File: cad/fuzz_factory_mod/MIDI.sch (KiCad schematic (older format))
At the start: 16 parts

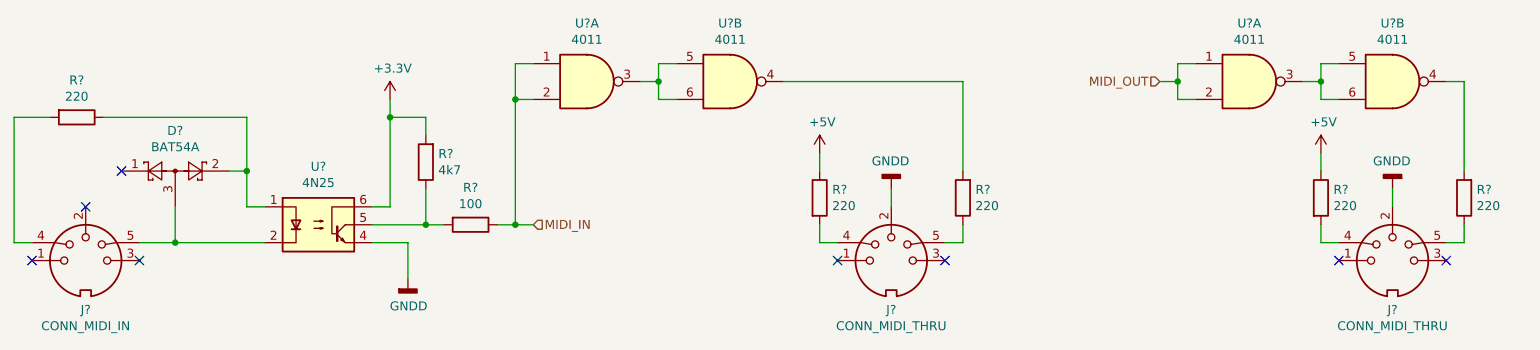
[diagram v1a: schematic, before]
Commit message: Continued schematic.
Modified fuuz_factory circuit : use of matched transistor pairs.
Added USB interface, through FT230X and direct to MCU.
Associated footprints, except for XTAL and trimmers.
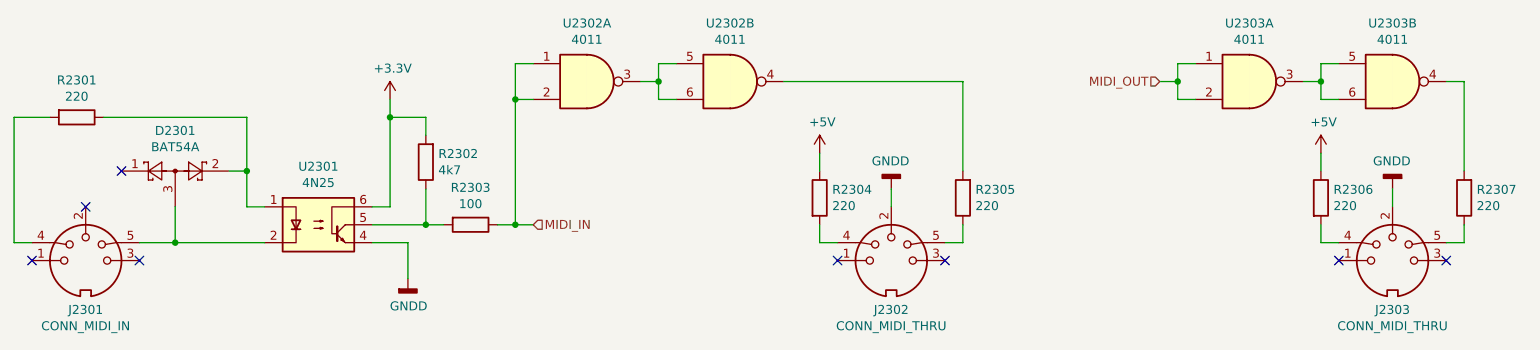
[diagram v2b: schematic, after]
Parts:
- J2301, J2302, J2303: renamed from J?; footprint (none) -> flax_lib:DIN5_through_hole
- R2301, R2304, R2305, R2306, R2307: renamed from R?; footprint (none) -> Resistors_SMD:R_0805
- R2302, R2303: renamed from R?; footprint (none) -> Resistors_SMD:R_0603
- U2302, U2303: renamed from U?; footprint (none) -> Housings_SOIC:SOIC-14_3.9x8.7mm_Pitch1.27mm
- gave numbers to parts that had none: 2
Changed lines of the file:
@@
 $Descr A4 11693 8268
 encoding utf-8
-Sheet 13 19
+Sheet 22 22
 Title ""
 Date ""
@@
 $EndDescr
 $Comp
-L Connector:DIN-5_180degree J?
+L Connector:DIN-5_180degree J2301
 U 1 1 5E67C58C
 P 2300 3500
-F 0 "J?" H 2300 3225 50  0000 C CNN
+F 0 "J2301" H 2300 3225 50  0000 C CNN
 F 1 "CONN_MIDI_IN" H 2300 3134 50  0000 C CNN
-F 2 "" H 2300 3500 50  0001 C CNN
+F 2 "flax_lib:DIN5_through_hole" H 2300 3500 50  0001 C CNN
 F 3 "http://www.mouser.com/ds/2/18/40_c091_abd_e-75918.pdf" H 2300 3500 50  0001 C CNN
 	1    2300 3500
@@
 $EndComp
 $Comp
-L Device:R R?
+L Device:R R2301
 U 1 1 5E67D871
 P 2250 2700
-F 0 "R?" V 2043 2700 50  0000 C CNN
+F 0 "R2301" V 2043 2700 50  0000 C CNN
 F 1 "220" V 2134 2700 50  0000 C CNN
-F 2 "" V 2180 2700 50  0001 C CNN
+F 2 "Resistors_SMD:R_0805" V 2180 2700 50  0001 C CNN
 F 3 "~" H 2250 2700 50  0001 C CNN
 	1    2250 2700
@@
 $EndComp
 $Comp
-L Diode:BAT54A D?
+L Diode:BAT54A D2301
 U 1 1 5E67E292
 P 2800 3000
-F 0 "D?" H 2800 3225 50  0000 C CNN
+F 0 "D2301" H 2800 3225 50  0000 C CNN
 F 1 "BAT54A" H 2800 3134 50  0000 C CNN
 F 2 "Package_TO_SOT_SMD:SOT-23" H 2875 3125 50  0001 L CNN
@@
 $EndComp
 $Comp
-L Isolator:4N25 U?
+L Isolator:4N25 U2301
 U 1 1 5E67F50F
 P 3600 3300
-F 0 "U?" H 3600 3625 50  0000 C CNN
+F 0 "U2301" H 3600 3625 50  0000 C CNN
 F 1 "4N25" H 3600 3534 50  0000 C CNN
 F 2 "Package_DIP:DIP-6_W7.62mm" H 3400 3100 50  0001 L CIN
@@
 Connection ~ 3200 3000
 $Comp
-L Device:R R?
+L Device:R R2302
 U 1 1 5E685D95
 P 4200 2950
-F 0 "R?" H 4130 2904 50  0000 R CNN
+F 0 "R2302" H 4130 2904 50  0000 R CNN
 F 1 "4k7" H 4130 2995 50  0000 R CNN
-F 2 "" V 4130 2950 50  0001 C CNN
+F 2 "Resistors_SMD:R_0603" V 4130 2950 50  0001 C CNN
 F 3 "~" H 4200 2950 50  0001 C CNN
 	1    4200 2950
@@
 $EndComp
 $Comp
-L Device:R R?
+L Device:R R2303
 U 1 1 5E6874F9
 P 4450 3300
-F 0 "R?" V 4243 3300 50  0000 C CNN
+F 0 "R2303" V 4243 3300 50  0000 C CNN
 F 1 "100" V 4334 3300 50  0000 C CNN
-F 2 "" V 4380 3300 50  0001 C CNN
+F 2 "Resistors_SMD:R_0603" V 4380 3300 50  0001 C CNN
 F 3 "~" H 4450 3300 50  0001 C CNN
 	1    4450 3300
@@
 	4200 3300 3900 3300
 $Comp
-L power:GNDD #PWR?
+L power:GNDD #PWR02302
 U 1 1 5E6887D9
 P 4100 3600
-F 0 "#PWR?" H 4100 3350 50  0001 C CNN
+F 0 "#PWR02302" H 4100 3350 50  0001 C CNN
 F 1 "GNDD" H 4104 3445 50  0000 C CNN
 F 2 "" H 4100 3600 50  0001 C CNN
@@
 	4600 3300 4700 3300
 $Comp
-L Connector:DIN-5_180degree J?
+L Connector:DIN-5_180degree J2302
 U 1 1 5E68C85A
 P 6800 3500
-F 0 "J?" H 6800 3225 50  0000 C CNN
+F 0 "J2302" H 6800 3225 50  0000 C CNN
 F 1 "CONN_MIDI_THRU" H 6800 3134 50  0000 C CNN
-F 2 "" H 6800 3500 50  0001 C CNN
+F 2 "flax_lib:DIN5_through_hole" H 6800 3500 50  0001 C CNN
 F 3 "http://www.mouser.com/ds/2/18/40_c091_abd_e-75918.pdf" H 6800 3500 50  0001 C CNN
 	1    6800 3500
@@
 $EndComp
 $Comp
-L 4xxx:4011 U?
+L 4xxx:4011 U2302
 U 1 1 5E68F415
 P 5100 2500
-F 0 "U?" H 5100 2825 50  0000 C CNN
+F 0 "U2302" H 5100 2825 50  0000 C CNN
 F 1 "4011" H 5100 2734 50  0000 C CNN
-F 2 "" H 5100 2500 50  0001 C CNN
+F 2 "Housings_SOIC:SOIC-14_3.9x8.7mm_Pitch1.27mm" H 5100 2500 50  0001 C CNN
 F 3 "http://www.intersil.com/content/dam/Intersil/documents/cd40/cd4011bms-12bms-23bms.pdf" H 5100 2500 50  0001 C CNN
 	1    5100 2500
@@
 $EndComp
 $Comp
-L 4xxx:4011 U?
+L 4xxx:4011 U2302
 U 2 1 5E692E59
 P 5900 2500
-F 0 "U?" H 5900 2825 50  0000 C CNN
+F 0 "U2302" H 5900 2825 50  0000 C CNN
 F 1 "4011" H 5900 2734 50  0000 C CNN
-F 2 "" H 5900 2500 50  0001 C CNN
+F 2 "Housings_SOIC:SOIC-14_3.9x8.7mm_Pitch1.27mm" H 5900 2500 50  0001 C CNN
 F 3 "http://www.intersil.com/content/dam/Intersil/documents/cd40/cd4011bms-12bms-23bms.pdf" H 5900 2500 50  0001 C CNN
 	2    5900 2500
@@
 	4700 3300 4800 3300
 $Comp
-L Device:R R?
+L Device:R R2304
 U 1 1 5E69AD62
 P 6400 3150
-F 0 "R?" H 6470 3196 50  0000 L CNN
+F 0 "R2304" H 6470 3196 50  0000 L CNN
 F 1 "220" H 6470 3105 50  0000 L CNN
-F 2 "" V 6330 3150 50  0001 C CNN
+F 2 "Resistors_SMD:R_0805" V 6330 3150 50  0001 C CNN
 F 3 "~" H 6400 3150 50  0001 C CNN
 	1    6400 3150
@@
 $EndComp
 $Comp
-L Device:R R?
+L Device:R R2305
 U 1 1 5E69C11A
 P 7200 3150
-F 0 "R?" H 7130 3104 50  0000 R CNN
+F 0 "R2305" H 7130 3104 50  0000 R CNN
 F 1 "220" H 7130 3195 50  0000 R CNN
-F 2 "" V 7130 3150 50  0001 C CNN
+F 2 "Resistors_SMD:R_0805" V 7130 3150 50  0001 C CNN
 F 3 "~" H 7200 3150 50  0001 C CNN
 	1    7200 3150
@@
 $EndComp
 $Comp
-L power:GNDD #PWR?
+L power:GNDD #PWR02304
 U 1 1 5E69CD49
 P 6800 3100
-F 0 "#PWR?" H 6800 2850 50  0001 C CNN
+F 0 "#PWR02304" H 6800 2850 50  0001 C CNN
 F 1 "GNDD" H 6804 2945 50  0000 C CNN
 F 2 "" H 6800 3100 50  0001 C CNN
@@
 	6400 3400 6500 3400
 $Comp
-L power:+5V #PWR?
+L power:+5V #PWR02303
 U 1 1 5E6A0890
 P 6400 2900
-F 0 "#PWR?" H 6400 2750 50  0001 C CNN
+F 0 "#PWR02303" H 6400 2750 50  0001 C CNN
 F 1 "+5V" H 6415 3073 50  0000 C CNN
 F 2 "" H 6400 2900 50  0001 C CNN
@@
 	7200 2500 7200 3000
 $Comp
-L 4xxx:4011 U?
+L 4xxx:4011 U2303
 U 1 1 5E6A2B71
 P 8800 2500
-F 0 "U?" H 8800 2825 50  0000 C CNN
+F 0 "U2303" H 8800 2825 50  0000 C CNN
 F 1 "4011" H 8800 2734 50  0000 C CNN
-F 2 "" H 8800 2500 50  0001 C CNN
+F 2 "Housings_SOIC:SOIC-14_3.9x8.7mm_Pitch1.27mm" H 8800 2500 50  0001 C CNN
 F 3 "http://www.intersil.com/content/dam/Intersil/documents/cd40/cd4011bms-12bms-23bms.pdf" H 8800 2500 50  0001 C CNN
 	1    8800 2500
@@
 $EndComp
 $Comp
-L 4xxx:4011 U?
+L 4xxx:4011 U2303
 U 2 1 5E6A2B7B
 P 9600 2500
-F 0 "U?" H 9600 2825 50  0000 C CNN
+F 0 "U2303" H 9600 2825 50  0000 C CNN
 F 1 "4011" H 9600 2734 50  0000 C CNN
-F 2 "" H 9600 2500 50  0001 C CNN
+F 2 "Housings_SOIC:SOIC-14_3.9x8.7mm_Pitch1.27mm" H 9600 2500 50  0001 C CNN
 F 3 "http://www.intersil.com/content/dam/Intersil/documents/cd40/cd4011bms-12bms-23bms.pdf" H 9600 2500 50  0001 C CNN
 	2    9600 2500
@@
 	9200 2500 9200 2600
 $Comp
-L Connector:DIN-5_180degree J?
+L Connector:DIN-5_180degree J2303
 U 1 1 5E6AB6C5
 P 9600 3500
-F 0 "J?" H 9600 3225 50  0000 C CNN
+F 0 "J2303" H 9600 3225 50  0000 C CNN
 F 1 "CONN_MIDI_THRU" H 9600 3134 50  0000 C CNN
-F 2 "" H 9600 3500 50  0001 C CNN
+F 2 "flax_lib:DIN5_through_hole" H 9600 3500 50  0001 C CNN
 F 3 "http://www.mouser.com/ds/2/18/40_c091_abd_e-75918.pdf" H 9600 3500 50  0001 C CNN
 	1    9600 3500
@@
 $EndComp
 $Comp
-L Device:R R?
+L Device:R R2306
 U 1 1 5E6AB6CF
 P 9200 3150
-F 0 "R?" H 9270 3196 50  0000 L CNN
+F 0 "R2306" H 9270 3196 50  0000 L CNN
 F 1 "220" H 9270 3105 50  0000 L CNN
-F 2 "" V 9130 3150 50  0001 C CNN
+F 2 "Resistors_SMD:R_0805" V 9130 3150 50  0001 C CNN
 F 3 "~" H 9200 3150 50  0001 C CNN
 	1    9200 3150
@@
 $EndComp
 $Comp
-L Device:R R?
+L Device:R R2307
 U 1 1 5E6AB6D9
 P 10000 3150
-F 0 "R?" H 9930 3104 50  0000 R CNN
+F 0 "R2307" H 9930 3104 50  0000 R CNN
 F 1 "220" H 9930 3195 50  0000 R CNN
-F 2 "" V 9930 3150 50  0001 C CNN
+F 2 "Resistors_SMD:R_0805" V 9930 3150 50  0001 C CNN
 F 3 "~" H 10000 3150 50  0001 C CNN
 	1    10000 3150
@@
 $EndComp
 $Comp
-L power:GNDD #PWR?
+L power:GNDD #PWR02306
 U 1 1 5E6AB6E3
 P 9600 3100
-F 0 "#PWR?" H 9600 2850 50  0001 C CNN
+F 0 "#PWR02306" H 9600 2850 50  0001 C CNN
 F 1 "GNDD" H 9604 2945 50  0000 C CNN
 F 2 "" H 9600 3100 50  0001 C CNN
@@
 	9200 3400 9300 3400
 $Comp
-L power:+5V #PWR?
+L power:+5V #PWR02305
 U 1 1 5E6AB6F4
 P 9200 2900
-F 0 "#PWR?" H 9200 2750 50  0001 C CNN
+F 0 "#PWR02305" H 9200 2750 50  0001 C CNN
 F 1 "+5V" H 9215 3073 50  0000 C CNN
 F 2 "" H 9200 2900 50  0001 C CNN
@@
 	8400 2500 8400 2600
 $Comp
-L power:+3.3V #PWR?
+L power:+3.3V #PWR02301
 U 1 1 5E6C550C
 P 4000 2600
-F 0 "#PWR?" H 4000 2450 50  0001 C CNN
+F 0 "#PWR02301" H 4000 2450 50  0001 C CNN
 F 1 "+3.3V" H 4015 2773 50  0000 C CNN
 F 2 "" H 4000 2600 50  0001 C CNN

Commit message: Continued schematic.
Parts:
- D2301: footprint Package_TO_SOT_SMD:SOT-23 -> TO_SOT_Packages_SMD:SOT-23
- U2301: footprint Package_DIP:DIP-6_W7.62mm -> Housings_DIP:DIP-6_W7.62mm
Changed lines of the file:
@@
 $Descr A4 11693 8268
 encoding utf-8
-Sheet 22 22
+Sheet 26 26
 Title ""
 Date ""
@@
 F 0 "D2301" H 2800 3225 50  0000 C CNN
 F 1 "BAT54A" H 2800 3134 50  0000 C CNN
-F 2 "Package_TO_SOT_SMD:SOT-23" H 2875 3125 50  0001 L CNN
+F 2 "TO_SOT_Packages_SMD:SOT-23" H 2875 3125 50  0001 L CNN
 F 3 "http://www.diodes.com/_files/datasheets/ds11005.pdf" H 2680 3000 50  0001 C CNN
 	1    2800 3000
@@
 F 0 "U2301" H 3600 3625 50  0000 C CNN
 F 1 "4N25" H 3600 3534 50  0000 C CNN
-F 2 "Package_DIP:DIP-6_W7.62mm" H 3400 3100 50  0001 L CIN
+F 2 "Housings_DIP:DIP-6_W7.62mm" H 3400 3100 50  0001 L CIN
 F 3 "https://www.vishay.com/docs/83725/4n25.pdf" H 3600 3300 50  0001 L CNN
 	1    3600 3300

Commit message: Continued schematic.
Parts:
- added C907: 100n, Capacitors_SMD:C_0603, symbol Device:C
- added unit 5 of U902
- J903: renamed from J2303; value CONN_MIDI_THRU -> CONN_MIDI_OUT
- renumbered D2301 to D901, J2301 to J901, J2302 to J902, R2301 to R917, R2302 to R918, R2303 to R919, R2304 to R920, R2305 to R921, R2306 to R922, R2307 to R923, U2301 to U901, U2302 to U902, U2303 to U902
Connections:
- net +5V: now also C907.2, U902.14 (VDD)
- net GNDD: now also C907.1, U902.7 (VSS)
- net MIDI_OUT: now also U902.8, U902.9; no longer U902.1, U902.2
- net at R923.2: now also U902.11; no longer U902.4
- new net: U902.10, U902.12, U902.13
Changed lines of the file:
@@
 $Descr A4 11693 8268
 encoding utf-8
-Sheet 26 26
+Sheet 9 30
 Title ""
 Date ""
@@
 $EndDescr
 $Comp
-L Connector:DIN-5_180degree J2301
+L Connector:DIN-5_180degree J901
 U 1 1 5E67C58C
 P 2300 3500
-F 0 "J2301" H 2300 3225 50  0000 C CNN
+F 0 "J901" H 2300 3225 50  0000 C CNN
 F 1 "CONN_MIDI_IN" H 2300 3134 50  0000 C CNN
 F 2 "flax_lib:DIN5_through_hole" H 2300 3500 50  0001 C CNN
@@
 $EndComp
 $Comp
-L Device:R R2301
+L Device:R R917
 U 1 1 5E67D871
 P 2250 2700
-F 0 "R2301" V 2043 2700 50  0000 C CNN
+F 0 "R917" V 2043 2700 50  0000 C CNN
 F 1 "220" V 2134 2700 50  0000 C CNN
 F 2 "Resistors_SMD:R_0805" V 2180 2700 50  0001 C CNN
@@
 $EndComp
 $Comp
-L Diode:BAT54A D2301
+L Diode:BAT54A D901
 U 1 1 5E67E292
 P 2800 3000
-F 0 "D2301" H 2800 3225 50  0000 C CNN
+F 0 "D901" H 2800 3225 50  0000 C CNN
 F 1 "BAT54A" H 2800 3134 50  0000 C CNN
 F 2 "TO_SOT_Packages_SMD:SOT-23" H 2875 3125 50  0001 L CNN
@@
 $EndComp
 $Comp
-L Isolator:4N25 U2301
+L Isolator:4N25 U901
 U 1 1 5E67F50F
 P 3600 3300
-F 0 "U2301" H 3600 3625 50  0000 C CNN
+F 0 "U901" H 3600 3625 50  0000 C CNN
 F 1 "4N25" H 3600 3534 50  0000 C CNN
 F 2 "Housings_DIP:DIP-6_W7.62mm" H 3400 3100 50  0001 L CIN
@@
 Connection ~ 3200 3000
 $Comp
-L Device:R R2302
+L Device:R R918
 U 1 1 5E685D95
 P 4200 2950
-F 0 "R2302" H 4130 2904 50  0000 R CNN
+F 0 "R918" H 4130 2904 50  0000 R CNN
 F 1 "4k7" H 4130 2995 50  0000 R CNN
 F 2 "Resistors_SMD:R_0603" V 4130 2950 50  0001 C CNN
@@
 $EndComp
 $Comp
-L Device:R R2303
+L Device:R R919
 U 1 1 5E6874F9
 P 4450 3300
-F 0 "R2303" V 4243 3300 50  0000 C CNN
+F 0 "R919" V 4243 3300 50  0000 C CNN
 F 1 "100" V 4334 3300 50  0000 C CNN
 F 2 "Resistors_SMD:R_0603" V 4380 3300 50  0001 C CNN
@@
 	4200 3300 3900 3300
 $Comp
-L power:GNDD #PWR02302
+L power:GNDD #PWR0241
 U 1 1 5E6887D9
 P 4100 3600
-F 0 "#PWR02302" H 4100 3350 50  0001 C CNN
+F 0 "#PWR0241" H 4100 3350 50  0001 C CNN
 F 1 "GNDD" H 4104 3445 50  0000 C CNN
 F 2 "" H 4100 3600 50  0001 C CNN
@@
 	4600 3300 4700 3300
 $Comp
-L Connector:DIN-5_180degree J2302
+L Connector:DIN-5_180degree J902
 U 1 1 5E68C85A
 P 6800 3500
-F 0 "J2302" H 6800 3225 50  0000 C CNN
+F 0 "J902" H 6800 3225 50  0000 C CNN
 F 1 "CONN_MIDI_THRU" H 6800 3134 50  0000 C CNN
 F 2 "flax_lib:DIN5_through_hole" H 6800 3500 50  0001 C CNN
@@
 $EndComp
 $Comp
-L 4xxx:4011 U2302
+L 4xxx:4011 U902
 U 1 1 5E68F415
 P 5100 2500
-F 0 "U2302" H 5100 2825 50  0000 C CNN
+F 0 "U902" H 5100 2825 50  0000 C CNN
 F 1 "4011" H 5100 2734 50  0000 C CNN
 F 2 "Housings_SOIC:SOIC-14_3.9x8.7mm_Pitch1.27mm" H 5100 2500 50  0001 C CNN
@@
 $EndComp
 $Comp
-L 4xxx:4011 U2302
+L 4xxx:4011 U902
 U 2 1 5E692E59
 P 5900 2500
-F 0 "U2302" H 5900 2825 50  0000 C CNN
+F 0 "U902" H 5900 2825 50  0000 C CNN
 F 1 "4011" H 5900 2734 50  0000 C CNN
 F 2 "Housings_SOIC:SOIC-14_3.9x8.7mm_Pitch1.27mm" H 5900 2500 50  0001 C CNN
@@
 	4700 3300 4800 3300
 $Comp
-L Device:R R2304
+L Device:R R920
 U 1 1 5E69AD62
 P 6400 3150
-F 0 "R2304" H 6470 3196 50  0000 L CNN
+F 0 "R920" H 6470 3196 50  0000 L CNN
 F 1 "220" H 6470 3105 50  0000 L CNN
 F 2 "Resistors_SMD:R_0805" V 6330 3150 50  0001 C CNN
@@
 $EndComp
 $Comp
-L Device:R R2305
+L Device:R R921
 U 1 1 5E69C11A
 P 7200 3150
-F 0 "R2305" H 7130 3104 50  0000 R CNN
+F 0 "R921" H 7130 3104 50  0000 R CNN
 F 1 "220" H 7130 3195 50  0000 R CNN
 F 2 "Resistors_SMD:R_0805" V 7130 3150 50  0001 C CNN
@@
 $EndComp
 $Comp
-L power:GNDD #PWR02304
+L power:GNDD #PWR0242
 U 1 1 5E69CD49
 P 6800 3100
-F 0 "#PWR02304" H 6800 2850 50  0001 C CNN
+F 0 "#PWR0242" H 6800 2850 50  0001 C CNN
 F 1 "GNDD" H 6804 2945 50  0000 C CNN
 F 2 "" H 6800 3100 50  0001 C CNN
@@
 	6400 3400 6500 3400
 $Comp
-L power:+5V #PWR02303
+L power:+5V #PWR0243
 U 1 1 5E6A0890
 P 6400 2900
-F 0 "#PWR02303" H 6400 2750 50  0001 C CNN
+F 0 "#PWR0243" H 6400 2750 50  0001 C CNN
 F 1 "+5V" H 6415 3073 50  0000 C CNN
 F 2 "" H 6400 2900 50  0001 C CNN
@@
 	7200 2500 7200 3000
 $Comp
-L 4xxx:4011 U2303
-U 1 1 5E6A2B71
+L 4xxx:4011 U902
+U 3 1 5E6A2B71
 P 8800 2500
-F 0 "U2303" H 8800 2825 50  0000 C CNN
+F 0 "U902" H 8800 2825 50  0000 C CNN
 F 1 "4011" H 8800 2734 50  0000 C CNN
 F 2 "Housings_SOIC:SOIC-14_3.9x8.7mm_Pitch1.27mm" H 8800 2500 50  0001 C CNN
 F 3 "http://www.intersil.com/content/dam/Intersil/documents/cd40/cd4011bms-12bms-23bms.pdf" H 8800 2500 50  0001 C CNN
-	1    8800 2500
-	1    0    0    -1
-$EndComp
-$Comp
-L 4xxx:4011 U2303
-U 2 1 5E6A2B7B
+	3    8800 2500
+	1    0    0    -1
+$EndComp
+$Comp
+L 4xxx:4011 U902
+U 4 1 5E6A2B7B
 P 9600 2500
-F 0 "U2303" H 9600 2825 50  0000 C CNN
+F 0 "U902" H 9600 2825 50  0000 C CNN
 F 1 "4011" H 9600 2734 50  0000 C CNN
 F 2 "Housings_SOIC:SOIC-14_3.9x8.7mm_Pitch1.27mm" H 9600 2500 50  0001 C CNN
 F 3 "http://www.intersil.com/content/dam/Intersil/documents/cd40/cd4011bms-12bms-23bms.pdf" H 9600 2500 50  0001 C CNN
-	2    9600 2500
+	4    9600 2500
 	1    0    0    -1
 $EndComp
@@
 	9200 2500 9200 2600
 $Comp
-L Connector:DIN-5_180degree J2303
+L Connector:DIN-5_180degree J903
 U 1 1 5E6AB6C5
 P 9600 3500
-F 0 "J2303" H 9600 3225 50  0000 C CNN
-F 1 "CONN_MIDI_THRU" H 9600 3134 50  0000 C CNN
+F 0 "J903" H 9600 3225 50  0000 C CNN
+F 1 "CONN_MIDI_OUT" H 9600 3134 50  0000 C CNN
 F 2 "flax_lib:DIN5_through_hole" H 9600 3500 50  0001 C CNN
 F 3 "http://www.mouser.com/ds/2/18/40_c091_abd_e-75918.pdf" H 9600 3500 50  0001 C CNN
@@
 $EndComp
 $Comp
-L Device:R R2306
+L Device:R R922
 U 1 1 5E6AB6CF
 P 9200 3150
-F 0 "R2306" H 9270 3196 50  0000 L CNN
+F 0 "R922" H 9270 3196 50  0000 L CNN
 F 1 "220" H 9270 3105 50  0000 L CNN
 F 2 "Resistors_SMD:R_0805" V 9130 3150 50  0001 C CNN
@@
 $EndComp
 $Comp
-L Device:R R2307
+L Device:R R923
 U 1 1 5E6AB6D9
 P 10000 3150
-F 0 "R2307" H 9930 3104 50  0000 R CNN
+F 0 "R923" H 9930 3104 50  0000 R CNN
 F 1 "220" H 9930 3195 50  0000 R CNN
 F 2 "Resistors_SMD:R_0805" V 9930 3150 50  0001 C CNN
@@
 $EndComp
 $Comp
-L power:GNDD #PWR02306
+L power:GNDD #PWR0244
 U 1 1 5E6AB6E3
 P 9600 3100
-F 0 "#PWR02306" H 9600 2850 50  0001 C CNN
+F 0 "#PWR0244" H 9600 2850 50  0001 C CNN
 F 1 "GNDD" H 9604 2945 50  0000 C CNN
 F 2 "" H 9600 3100 50  0001 C CNN
@@
 	9200 3400 9300 3400
 $Comp
-L power:+5V #PWR02305
+L power:+5V #PWR0245
 U 1 1 5E6AB6F4
 P 9200 2900
-F 0 "#PWR02305" H 9200 2750 50  0001 C CNN
+F 0 "#PWR0245" H 9200 2750 50  0001 C CNN
 F 1 "+5V" H 9215 3073 50  0000 C CNN
 F 2 "" H 9200 2900 50  0001 C CNN
@@
 	8400 2500 8400 2600
 $Comp
-L power:+3.3V #PWR02301
+L power:+3.3V #PWR0246
 U 1 1 5E6C550C
 P 4000 2600
-F 0 "#PWR02301" H 4000 2450 50  0001 C CNN
+F 0 "#PWR0246" H 4000 2450 50  0001 C CNN
 F 1 "+3.3V" H 4015 2773 50  0000 C CNN
 F 2 "" H 4000 2600 50  0001 C CNN
@@
 	1    0    0    -1
 $EndComp
+$Comp
+L 4xxx:4011 U902
+U 5 1 5ECCC4D2
+P 4500 5000
+F 0 "U902" H 4650 5350 50  0000 C CNN
+F 1 "4011" H 4650 4650 50  0000 C CNN
+F 2 "Housings_SOIC:SOIC-14_3.9x8.7mm_Pitch1.27mm" H 4500 5000 50  0001 C CNN
+F 3 "http://www.intersil.com/content/dam/Intersil/documents/cd40/cd4011bms-12bms-23bms.pdf" H 4500 5000 50  0001 C CNN
+	5    4500 5000
+	1    0    0    -1
+$EndComp
+$Comp
+L power:+5V #PWR0905
+U 1 1 5ECCF353
+P 4500 4300
+F 0 "#PWR0905" H 4500 4150 50  0001 C CNN
+F 1 "+5V" H 4515 4473 50  0000 C CNN
+F 2 "" H 4500 4300 50  0001 C CNN
+F 3 "" H 4500 4300 50  0001 C CNN
+	1    4500 4300
+	1    0    0    -1
+$EndComp
+$Comp
+L power:GNDD #PWR0906
+U 1 1 5ECD1951
+P 4500 5600
+F 0 "#PWR0906" H 4500 5350 50  0001 C CNN
+F 1 "GNDD" H 4504 5445 50  0000 C CNN
+F 2 "" H 4500 5600 50  0001 C CNN
+F 3 "" H 4500 5600 50  0001 C CNN
+	1    4500 5600
+	1    0    0    -1
+$EndComp
+Wire Wire Line
+	4500 5500 4500 5600
+$Comp
+L Device:C C907
+U 1 1 5ECD322E
+P 4750 4400
+F 0 "C907" V 4498 4400 50  0000 C CNN
+F 1 "100n" V 4589 4400 50  0000 C CNN
+F 2 "Capacitors_SMD:C_0603" H 4788 4250 50  0001 C CNN
+F 3 "~" H 4750 4400 50  0001 C CNN
+	1    4750 4400
+	0    1    1    0
+$EndComp
+Wire Wire Line
+	4500 4300 4500 4400
+Wire Wire Line
+	4600 4400 4500 4400
+Connection ~ 4500 4400
+Wire Wire Line
+	4500 4400 4500 4500
+$Comp
+L power:GNDD #PWR0907
+U 1 1 5ECD67FD
+P 5000 4400
+F 0 "#PWR0907" H 5000 4150 50  0001 C CNN
+F 1 "GNDD" H 5004 4245 50  0000 C CNN
+F 2 "" H 5000 4400 50  0001 C CNN
+F 3 "" H 5000 4400 50  0001 C CNN
+	1    5000 4400
+	0    -1   -1   0
+$EndComp
+Wire Wire Line
+	5000 4400 4900 4400
 $EndSCHEMATC
